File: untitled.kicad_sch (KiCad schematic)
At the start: 51 parts

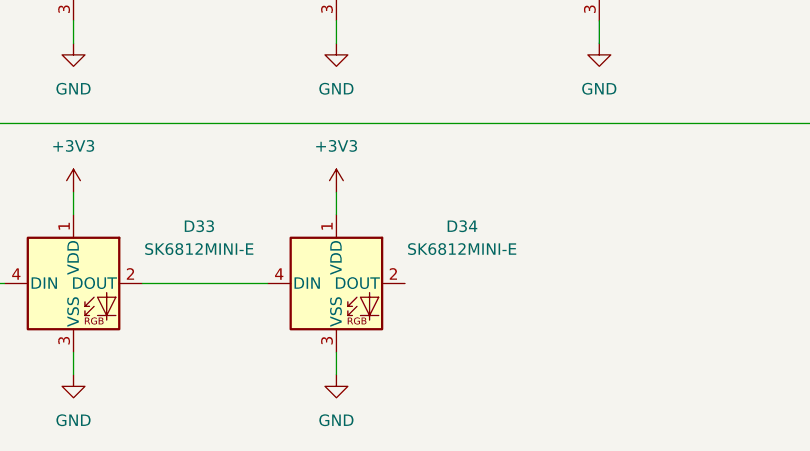
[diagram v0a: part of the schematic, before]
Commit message: Se hacen modificaciones en la pcb acomodando los dispositivos y se agrega tierra comun en ambos lados de la placa
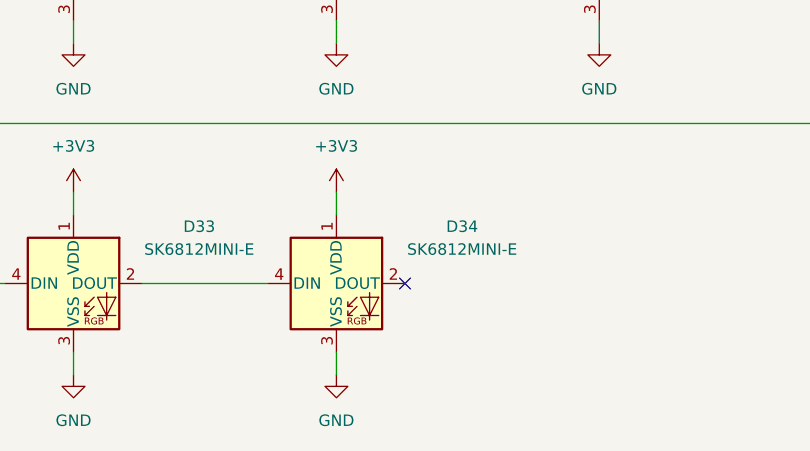
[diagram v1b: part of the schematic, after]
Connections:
- no-connect marks 0 -> 1
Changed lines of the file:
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@@
 		(color 0 0 0 0)
 	)
+	(no_connect
+		(at 72.39 181.61)
+	)
 	(wire
 		(pts
@@
 	(wire
 		(pts
+			(xy 222.25 33.02) (xy 222.25 34.29)
+		)
+		(stroke
+			(width 0)
+			(type default)
+		)
+	)
+	(wire
+		(pts
+			(xy 213.36 27.94) (xy 213.36 39.37)
+		)
+		(stroke
+			(width 0)
+			(type default)
+		)
+	)
+	(wire
+		(pts
+			(xy 64.77 134.62) (xy 64.77 137.16)
+		)
+		(stroke
+			(width 0)
+			(type default)
+		)
+	)
+	(wire
+		(pts
+			(xy 21.59 144.78) (xy 27.94 144.78)
+		)
+		(stroke
+			(width 0)
+			(type default)
+		)
+	)
+	(wire
+		(pts
+			(xy 101.6 34.29) (xy 115.57 34.29)
+		)
+		(stroke
+			(width 0)
+			(type default)
+		)
+	)
+	(wire
+		(pts
+			(xy 208.28 83.82) (xy 208.28 71.12)
+		)
+		(stroke
+			(width 0)
+			(type default)
+		)
+	)
+	(wire
+		(pts
+			(xy 248.92 64.77) (xy 254 64.77)
+		)
+		(stroke
+			(width 0)
+			(type default)
+		)
+	)
+	(wire
+		(pts
+			(xy 276.86 90.17) (xy 267.97 90.17)
+		)
+		(stroke
+			(width 0)
+			(type default)
+		)
+	)
+	(wire
+		(pts
+			(xy 254 83.82) (xy 254 71.12)
+		)
+		(stroke
+			(width 0)
+			(type default)
+		)
+	)
+	(wire
+		(pts
+			(xy 254 90.17) (xy 245.11 90.17)
+		)
+		(stroke
+			(width 0)
+			(type default)
+		)
+	)
+	(wire
+		(pts
+			(xy 72.39 34.29) (xy 86.36 34.29)
+		)
+		(stroke
+			(width 0)
+			(type default)
+		)
+	)
+	(wire
+		(pts
+			(xy 35.56 134.62) (xy 35.56 137.16)
+		)
+		(stroke
+			(width 0)
+			(type default)
+		)
+	)
+	(wire
+		(pts
+			(xy 248.92 121.92) (xy 254 121.92)
+		)
+		(stroke
+			(width 0)
+			(type default)
+		)
+	)
+	(wire
+		(pts
+			(xy 130.81 34.29) (xy 135.89 34.29)
+		)
+		(stroke
+			(width 0)
+			(type default)
+		)
+	)
+	(wire
+		(pts
+			(xy 123.19 78.74) (xy 123.19 81.28)
+		)
+		(stroke
+			(width 0)
+			(type default)
+		)
+	)
+	(wire
+		(pts
 			(xy 93.98 134.62) (xy 93.98 137.16)
 		)
 		(stroke
-			(width 0)
-			(type default)
-		)
-	)
-	(wire
-		(pts
-			(xy 222.25 33.02) (xy 222.25 34.29)
-		)
-		(stroke
-			(width 0)
-			(type default)
-		)
-	)
-	(wire
-		(pts
-			(xy 213.36 27.94) (xy 213.36 39.37)
-		)
-		(stroke
-			(width 0)
-			(type default)
-		)
-	)
-	(wire
-		(pts
-			(xy 64.77 134.62) (xy 64.77 137.16)
-		)
-		(stroke
-			(width 0)
-			(type default)
-		)
-	)
-	(wire
-		(pts
-			(xy 21.59 144.78) (xy 27.94 144.78)
-		)
-		(stroke
-			(width 0)
-			(type default)
-		)
-	)
-	(wire
-		(pts
-			(xy 101.6 34.29) (xy 115.57 34.29)
-		)
-		(stroke
-			(width 0)
-			(type default)
-		)
-	)
-	(wire
-		(pts
-			(xy 208.28 83.82) (xy 208.28 71.12)
-		)
-		(stroke
-			(width 0)
-			(type default)
-		)
-	)
-	(wire
-		(pts
-			(xy 248.92 64.77) (xy 254 64.77)
-		)
-		(stroke
-			(width 0)
-			(type default)
-		)
-	)
-	(wire
-		(pts
-			(xy 276.86 90.17) (xy 267.97 90.17)
-		)
-		(stroke
-			(width 0)
-			(type default)
-		)
-	)
-	(wire
-		(pts
-			(xy 254 83.82) (xy 254 71.12)
-		)
-		(stroke
-			(width 0)
-			(type default)
-		)
-	)
-	(wire
-		(pts
-			(xy 254 90.17) (xy 245.11 90.17)
-		)
-		(stroke
-			(width 0)
-			(type default)
-		)
-	)
-	(wire
-		(pts
-			(xy 72.39 34.29) (xy 86.36 34.29)
-		)
-		(stroke
-			(width 0)
-			(type default)
-		)
-	)
-	(wire
-		(pts
-			(xy 35.56 134.62) (xy 35.56 137.16)
-		)
-		(stroke
-			(width 0)
-			(type default)
-		)
-	)
-	(wire
-		(pts
-			(xy 248.92 121.92) (xy 254 121.92)
-		)
-		(stroke
-			(width 0)
-			(type default)
-		)
-	)
-	(wire
-		(pts
-			(xy 130.81 34.29) (xy 135.89 34.29)
-		)
-		(stroke
-			(width 0)
-			(type default)
-		)
-	)
-	(wire
-		(pts
-			(xy 123.19 78.74) (xy 123.19 81.28)
-		)
-		(stroke
